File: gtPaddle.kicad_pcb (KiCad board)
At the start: 2 copper layers, 51.4 x 72.6 mm, 26 parts, among them IC1 74157N, IC2 74157N, J1 Conn_01x02_Pin, J2 Conn_01x02_Pin, J3 Conn_01x02_Pin, J4 Conn_01x02_Pin, Q1 2N3904, U1 ADC0804LCN

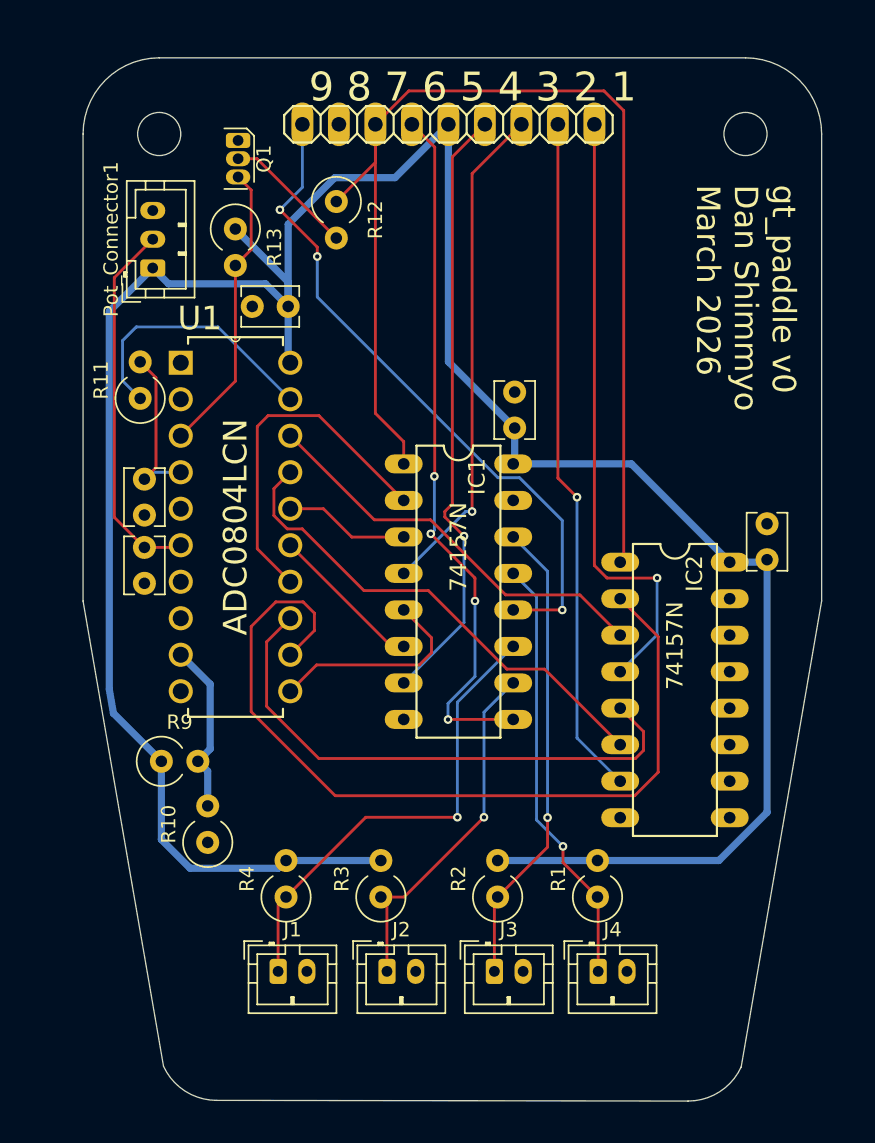
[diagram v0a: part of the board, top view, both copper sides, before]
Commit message: clean up traces, add vias
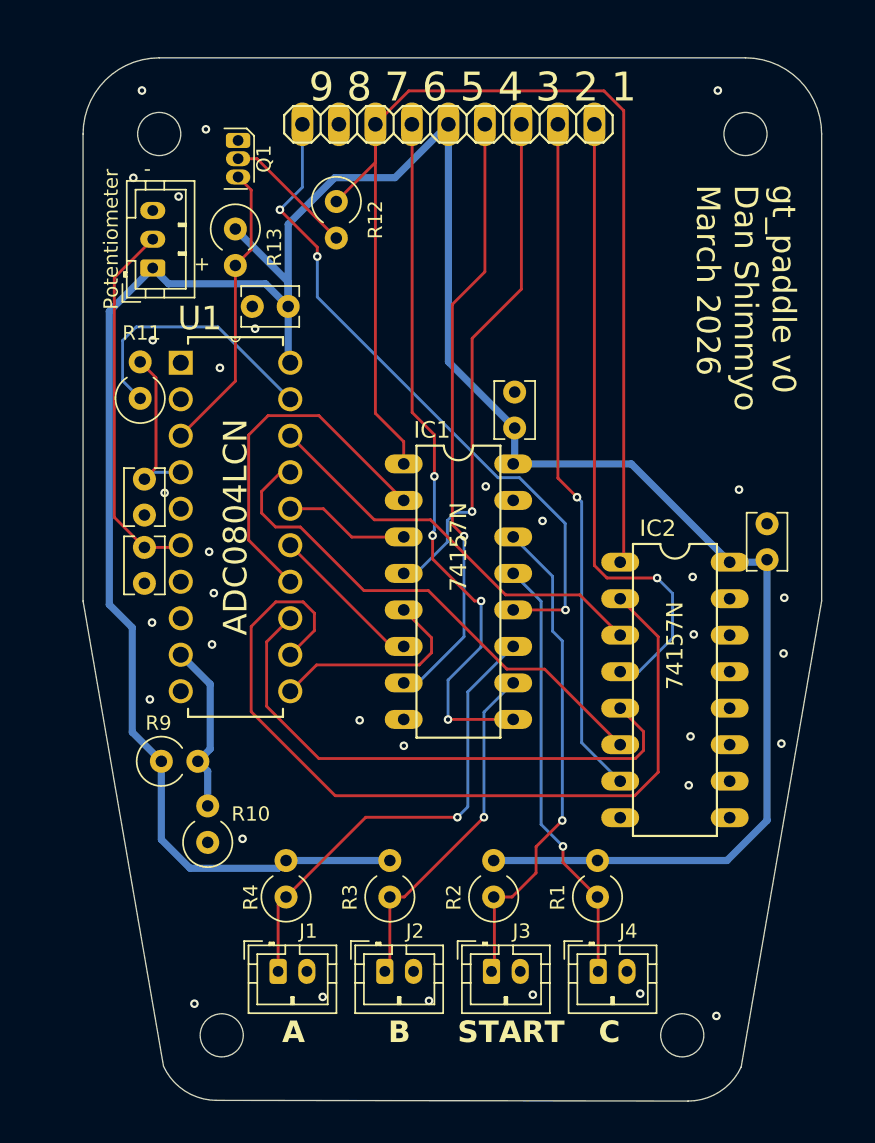
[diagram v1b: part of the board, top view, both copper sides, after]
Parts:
- added ?: , , F.Cu at (135.1, 135.6)
- added ?: , , F.Cu at (167.1, 135.6)
- moved R3 0.62 mm to (146.8, 126.0)
- moved R2 0.28 mm to (154.0, 126.0)
- moved J3 0.20 mm to (153.8, 131.2)
- moved J2 0.15 mm to (146.4, 131.2)
- renumbered Pot_Connector1 to Potentiometer
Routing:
- net Net-(IC2A-1Y): track 43.1 -> 44.7 mm
- net Net-(IC1A-4A): track 32.8 -> 34.4 mm
- net Net-(IC2A-2B): track 34.2 -> 35.7 mm
- net VCC: track 183.8 -> 185.1 mm
- net Net-(IC1A-1Y): track 34.9 -> 35.8 mm
- net Net-(IC1A-3B): track 25.0 -> 24.4 mm
- net Net-(IC1A-3Y): track 48.8 -> 49.3 mm
- net GND: vias 0 -> 33
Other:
- board text added: "+"
- board text added: "-"
- board text added: "A"
- board text added: "B"
- board text added: "C"
- board text added: "START"

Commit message: enough edits for one night
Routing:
- net Net-(IC2A-1Y): track 44.7 -> 46.2 mm
- net VCC: track 185.1 -> 186.4 mm
- net GND: vias 33 -> 44

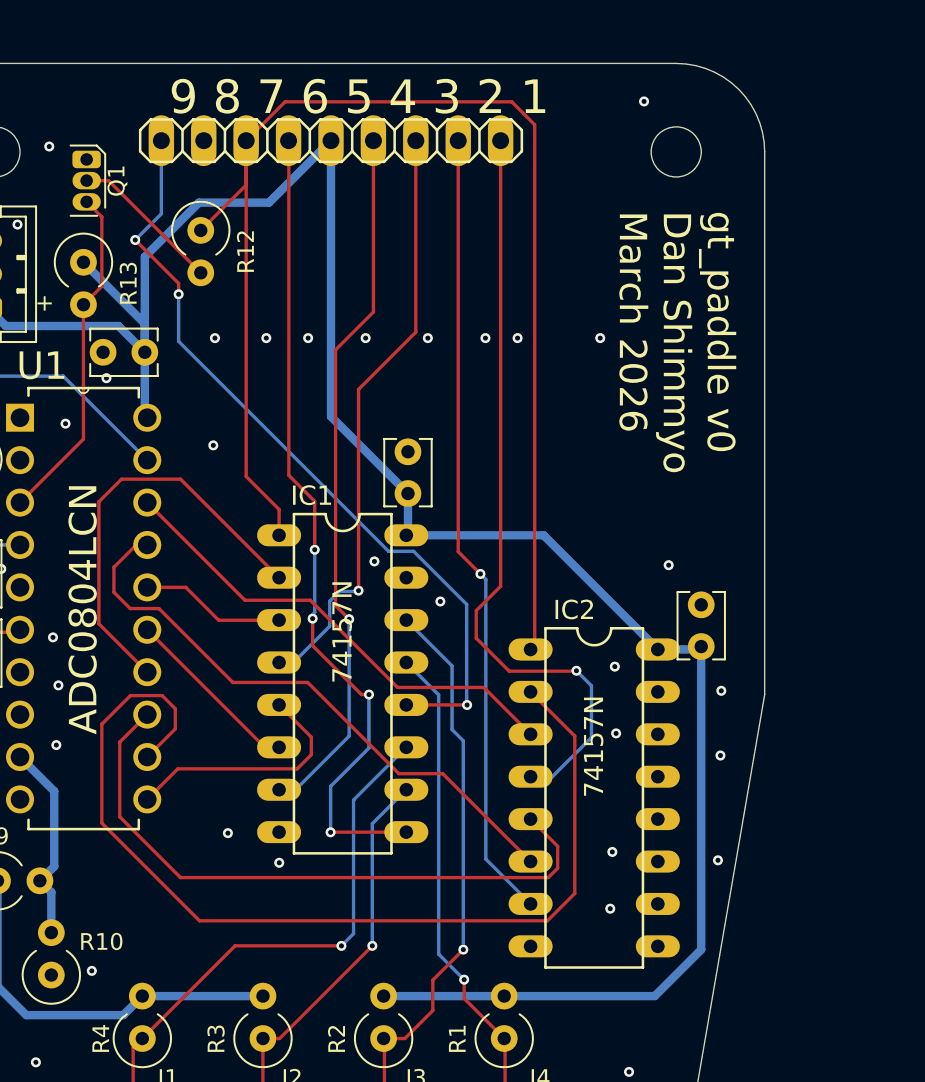
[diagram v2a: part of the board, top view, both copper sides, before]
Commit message: muxes moved up
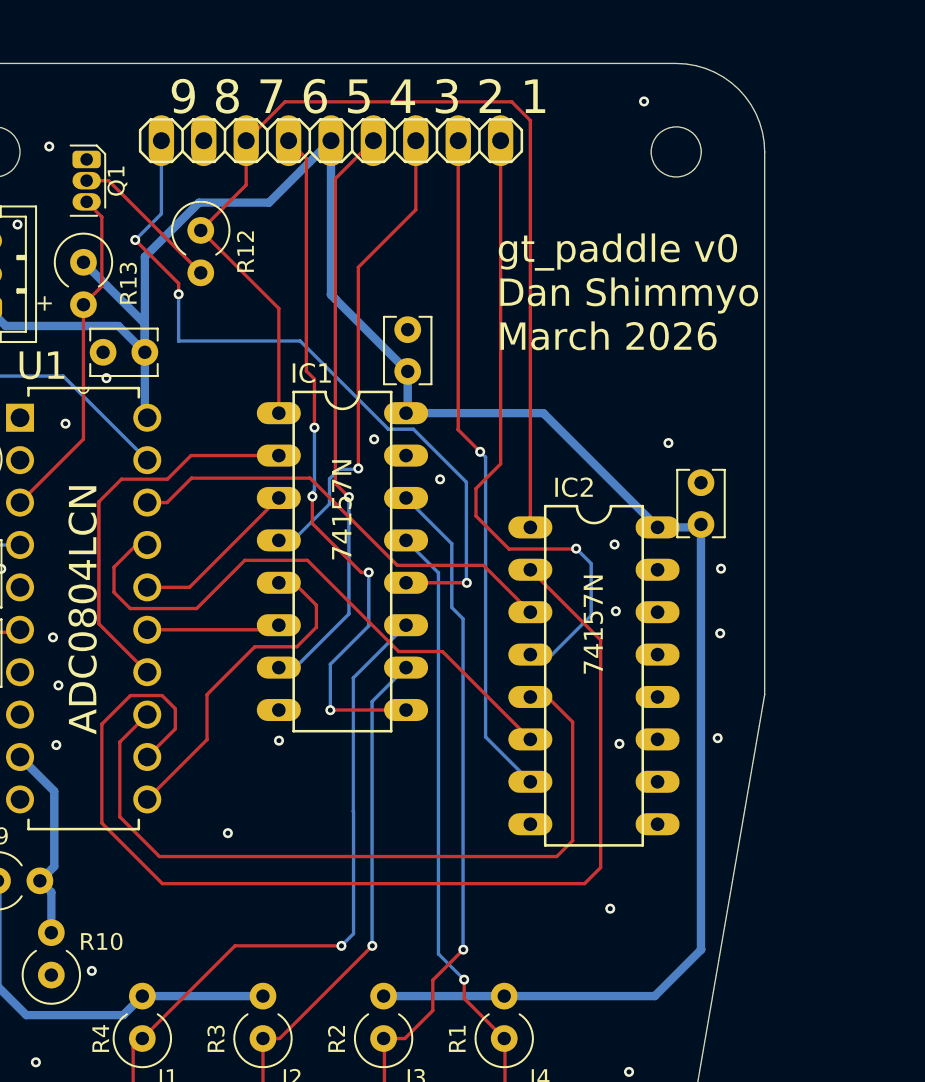
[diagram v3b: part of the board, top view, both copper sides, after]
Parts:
- moved C3 7.32 mm to (173.0, 95.2)
- moved C4 7.32 mm to (155.4, 86.0)
- moved IC1 7.32 mm to (151.5, 97.4)
- moved IC2 7.32 mm to (166.6, 104.3)
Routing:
- net Net-(IC1A-~{A}/B): track 81.3 -> 62.6 mm
- net Net-(IC1A-4B): track 30.1 -> 37.5 mm
- net Net-(IC1A-4A): track 34.4 -> 41.7 mm
- net Net-(IC1A-3B): track 24.4 -> 31.8 mm
- net Net-(IC1A-3A): track 33.2 -> 40.5 mm
- net Net-(IC2A-2Y): track 47.6 -> 40.3 mm
- net Net-(IC2A-1Y): track 46.2 -> 38.9 mm
- net Net-(IC1A-2Y): track 42.5 -> 35.2 mm
- net Net-(IC1A-1Y): track 35.8 -> 28.5 mm
- net Net-(IC1A-3Y): track 49.3 -> 42.0 mm
- net Net-(IC2A-2A): track 38.4 -> 45.6 mm
- net Net-(IC2A-1A): track 59.5 -> 66.3 mm
- net Net-(IC1A-2A): track 14.7 -> 20.1 mm
- net Net-(IC1A-4Y): track 47.2 -> 44.2 mm
- net Net-(IC1A-2B): track 10.8 -> 8.38 mm
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
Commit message: Individual headers first pass
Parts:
- removed ? (x4): , 
- removed Potentiometer: Conn_01x03_Pin, Connector_JST:JST_PH_B3B-PH-K_1x03_P2.00mm_Vertical
- added JP2: Conn_01x01_Socket, Connector_Wire:SolderWire-0.75sqmm_1x01_D1.25mm_OD2.3mm, F.Cu at (168.6, 86.2)
- added JP3: Conn_01x01_Socket, Connector_Wire:SolderWire-0.75sqmm_1x01_D1.25mm_OD2.3mm, F.Cu at (164.7, 85.5)
- added JP4: Conn_01x01_Socket, Connector_Wire:SolderWire-0.75sqmm_1x01_D1.25mm_OD2.3mm, F.Cu at (161.6, 81.6)
- added JP5: Conn_01x01_Socket, Connector_Wire:SolderWire-0.75sqmm_1x01_D1.25mm_OD2.3mm, F.Cu at (155.2, 79.5)
- added JP6: Conn_01x01_Socket, Connector_Wire:SolderWire-0.75sqmm_1x01_D1.25mm_OD2.3mm, F.Cu at (149.8, 78.6)
- added JP7: Conn_01x01_Socket, Connector_Wire:SolderWire-0.75sqmm_1x01_D1.25mm_OD2.3mm, F.Cu at (146.9, 74.3)
- added JP8: Conn_01x01_Socket, Connector_Wire:SolderWire-0.75sqmm_1x01_D1.25mm_OD2.3mm, F.Cu at (141.1, 72.3)
- added JP9: Conn_01x01_Socket, Connector_Wire:SolderWire-0.75sqmm_1x01_D1.25mm_OD2.3mm, F.Cu at (142.7, 84.3)
- added Pot_Connector1: Conn_01x03_Pin, Connector_JST:JST_PH_B3B-PH-K_1x03_P2.00mm_Vertical, F.Cu at (130.2, 82.2)
- JP1: value PINHD-1X9 -> Conn_01x01_Socket; footprint gpad1:1X09 -> Connector_Wire:SolderWire-0.75sqmm_1x01_D1.25mm_OD2.3mm
- moved JP1 26.4 mm to (172.5, 87.2)
- turned C4 to 0 degrees
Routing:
- net Net-(IC1A-~{A}/B): track 62.6 -> 42.3 mm, vias 0 -> 1
- net Net-(IC2A-1Y): track 38.9 -> 20.5 mm
- net Net-(IC1A-4Y): track 44.2 -> 29.4 mm, vias 3 -> 1
- net VCC: track 186.8 -> 176.2 mm
- net Net-(IC2A-2Y): track 40.3 -> 31.8 mm
- net Net-(IC1A-3Y): track 42.0 -> 36.9 mm
- net Net-(IC1A-1Y): track 28.5 -> 27.7 mm
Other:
- board text removed: "1 2 3 4 5 6 7 8 9"
- board text removed: "9 8 7 6 5 4 3 2 1"

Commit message: spent too much time fanning out the headers
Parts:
- moved JP9 12.9 mm to (144.7, 71.5)
- moved JP8 7.62 mm to (148.6, 73.6)
- moved JP7 5.61 mm to (150.2, 78.8)
- moved JP6 4.49 mm to (154.2, 79.7)
- moved C4 3.83 mm to (158.4, 88.5), turned to 90 degrees
- moved JP5 3.79 mm to (158.1, 81.9)
- moved JP4 2.89 mm to (161.8, 84.5)
- moved JP2 2.54 mm to (169.7, 88.5)
- moved JP1 2.49 mm to (173.5, 89.5)
- moved JP3 1.47 mm to (165.7, 86.6)
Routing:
- net Net-(IC1A-4Y): track 29.4 -> 37.9 mm, vias 1 -> 2
- net Net-(IC1A-1Y): track 27.7 -> 23.3 mm
- net VCC: track 176.2 -> 172.2 mm
- net Net-(IC2A-2Y): track 31.8 -> 29.1 mm
- net Net-(IC1A-2Y): track 35.3 -> 32.9 mm
- net Net-(IC1A-~{A}/B): track 42.3 -> 44.2 mm, vias 1 -> 2
- net Net-(IC2A-1Y): track 20.5 -> 19.2 mm
- net Net-(IC1A-3Y): track 36.9 -> 35.7 mm

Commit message: angular shape
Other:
- outline, holes or cut-outs redrawn

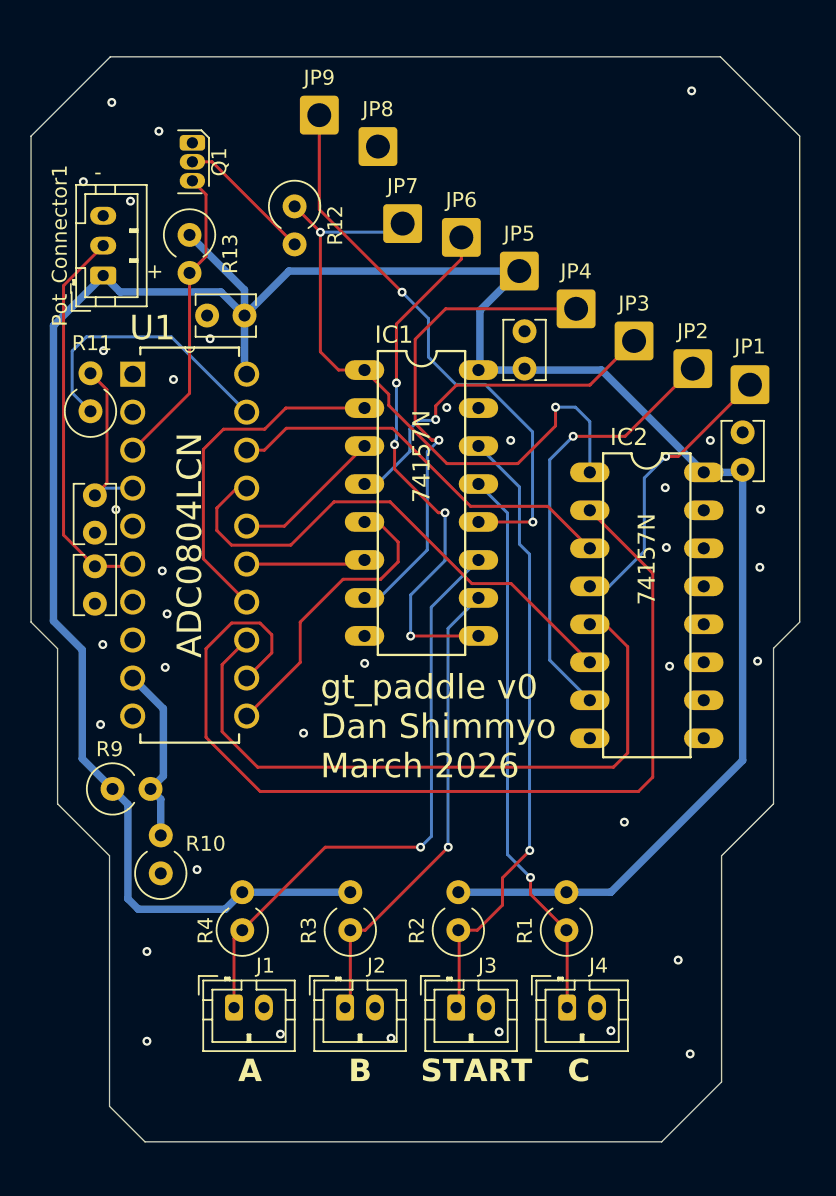
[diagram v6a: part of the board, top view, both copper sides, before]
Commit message: moved teeth up
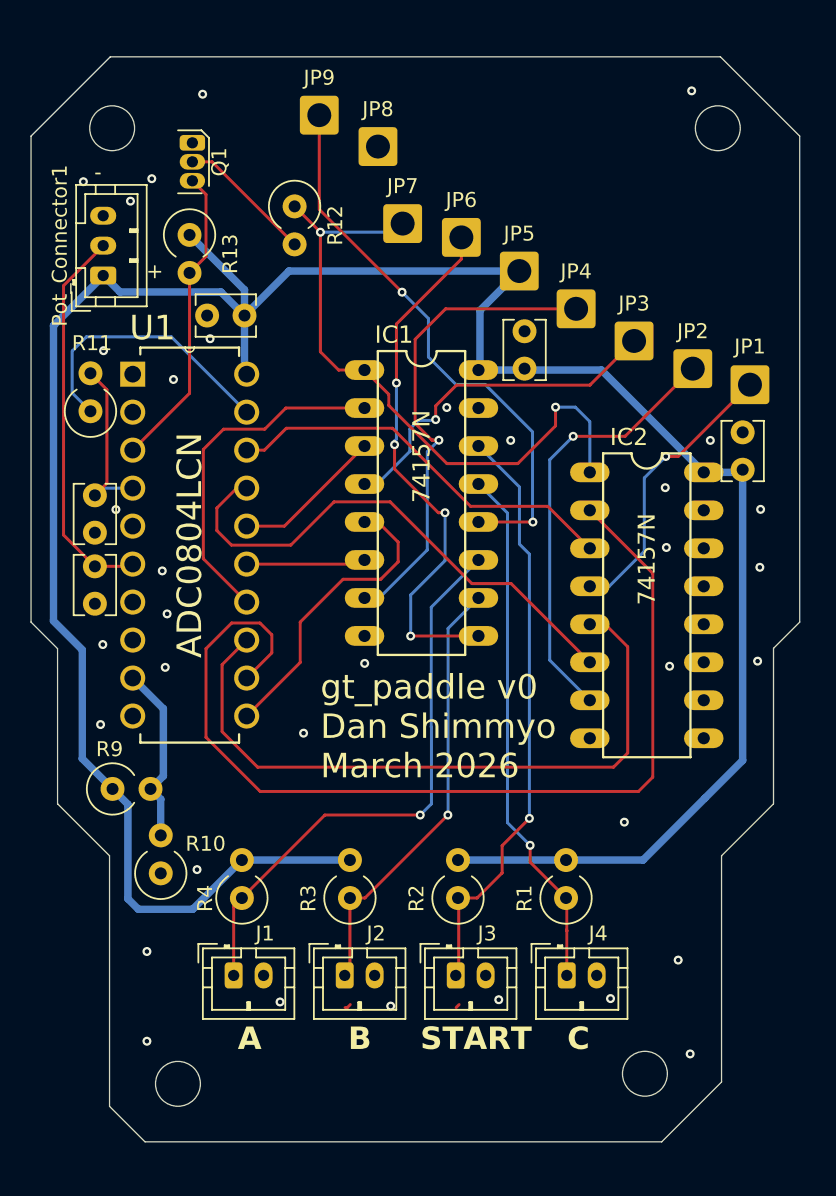
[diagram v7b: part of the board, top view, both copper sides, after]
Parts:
- added REF**: MountingHole_3mm, MountingHole:MountingHole_3mm, F.Cu at (130.8, 72.4)
- added REF**: MountingHole_3mm, MountingHole:MountingHole_3mm, F.Cu at (135.2, 136.3)
- added REF**: MountingHole_3mm, MountingHole:MountingHole_3mm, F.Cu at (166.4, 135.6)
- added REF**: MountingHole_3mm, MountingHole:MountingHole_3mm, F.Cu at (171.3, 72.4)
- moved J1 2.15 mm to (138.9, 129.0)
- moved J2 2.15 mm to (146.4, 129.0)
- moved J3 2.15 mm to (153.8, 129.0)
- moved J4 2.15 mm to (161.2, 129.0)
- moved R1 2.15 mm to (161.2, 123.8)
- moved R2 2.15 mm to (153.9, 123.8)
- moved R3 2.15 mm to (146.7, 123.8)
- moved R4 2.15 mm to (139.5, 123.8)
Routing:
- net Net-(IC1A-3A): track 40.5 -> 38.3 mm
- net Net-(IC1A-4B): track 37.5 -> 35.3 mm
- net Net-(IC1A-3B): track 31.8 -> 29.6 mm
- net Net-(IC1A-4A): track 41.7 -> 39.6 mm

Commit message: checking edge cuts and mounting points
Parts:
- moved REF** 0.40 mm to (166.5, 136.0)
- moved REF** 0.36 mm to (135.0, 136.0)
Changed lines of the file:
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@@
 	(footprint "MountingHole:MountingHole_3mm"
 		(layer "F.Cu")
-		(at 135.225 136.275)
+		(at 135 136)
 		(descr "Mounting Hole 3mm, no annular, generated by kicad-footprint-generator mountinghole.py")
 		(tags "mountinghole")
@@
 	(footprint "MountingHole:MountingHole_3mm"
 		(layer "F.Cu")
-		(at 166.45 135.6)
+		(at 166.5 136)
 		(descr "Mounting Hole 3mm, no annular, generated by kicad-footprint-generator mountinghole.py")
 		(tags "mountinghole")
